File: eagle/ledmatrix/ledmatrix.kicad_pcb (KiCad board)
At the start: 2 copper layers, 100 x 160 mm, 65 parts, among them P1 CONN_01X05, P2 CONN_01X05, Q1 BSS138, Q10 BSS138, Q11 BSS138, Q12 BSS138, Q13 BSS138, Q14 BSS138, Q15 BSS138, Q16 BSS138, Q17 BSS138, Q18 BSS138, Q19 BSS138, Q2 BSS138, Q20 BSS138, Q3 BSS138, Q4 BSS138, Q5 BSS138, Q6 BSS138, Q7 BSS138, Q8 BSS138, Q9 BSS138, U1 74HC595, U2 74HC595, U3 74HC595

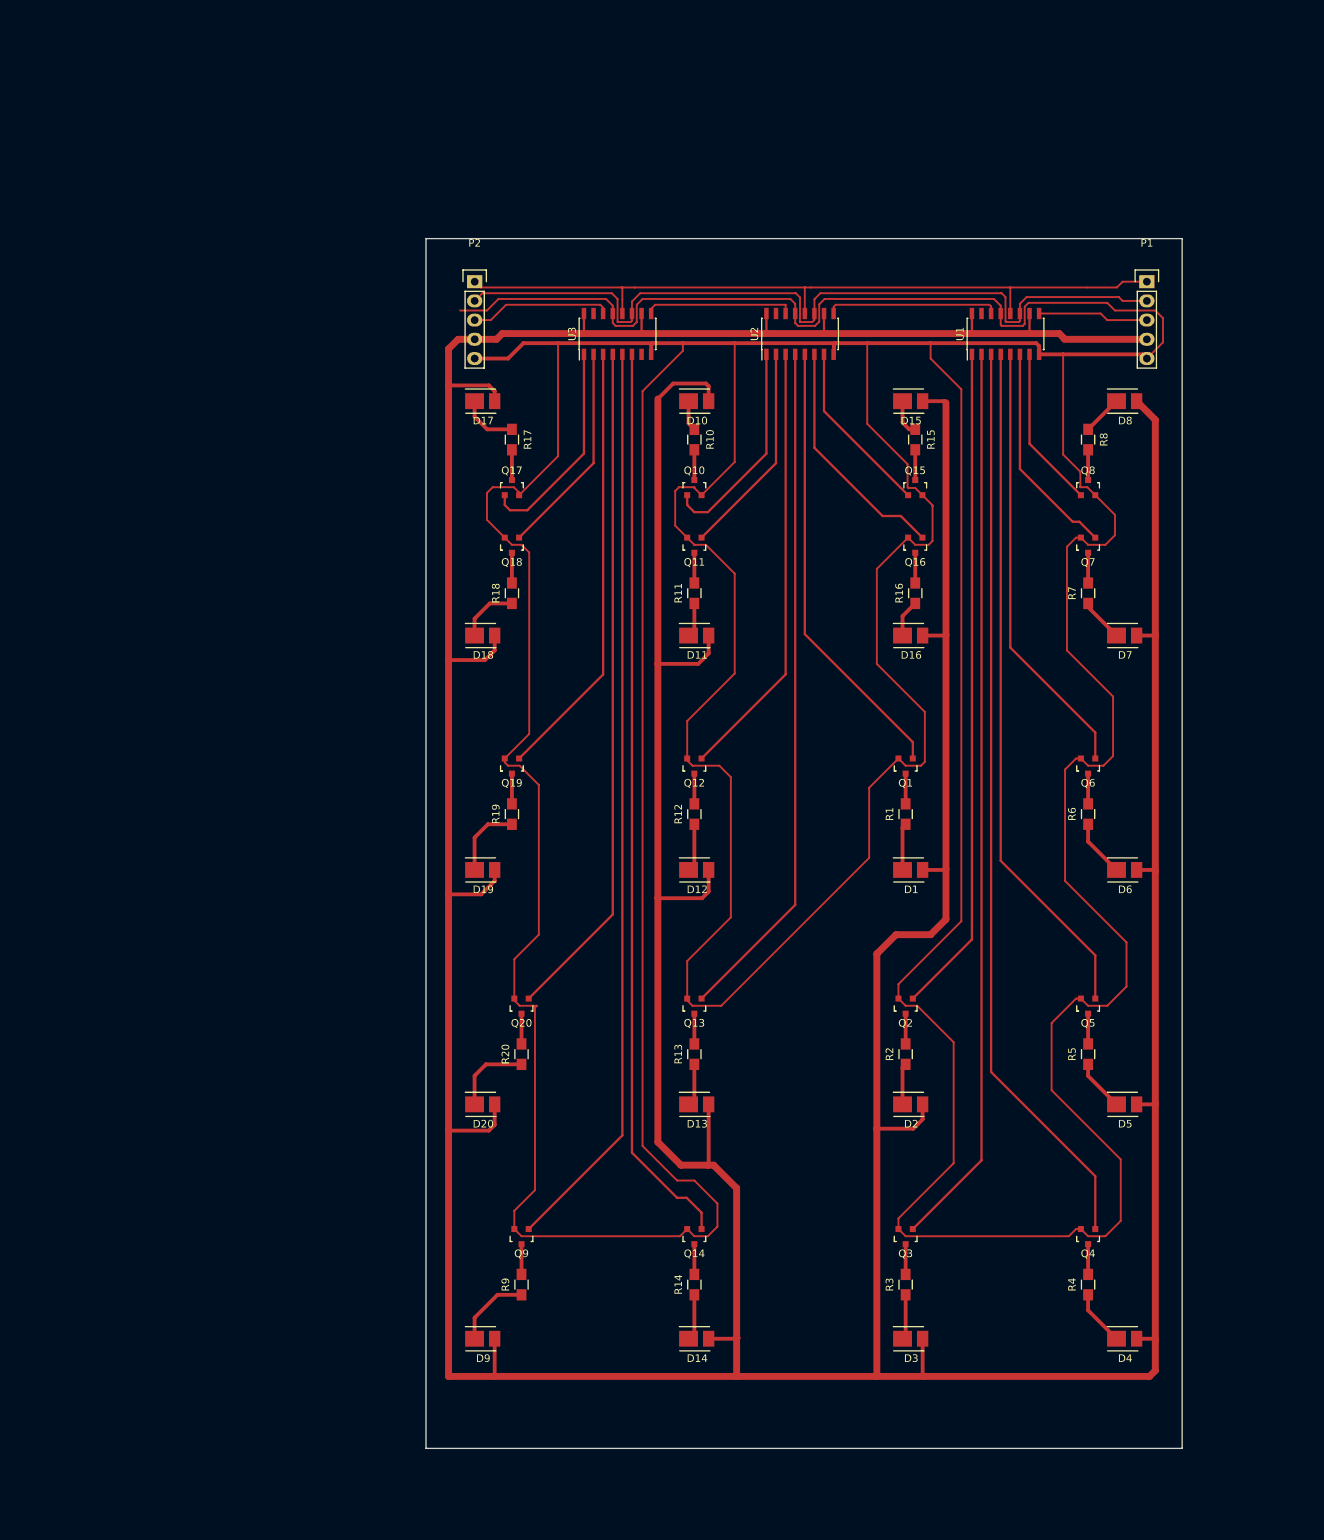
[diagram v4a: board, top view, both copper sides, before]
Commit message: adds ground fill.
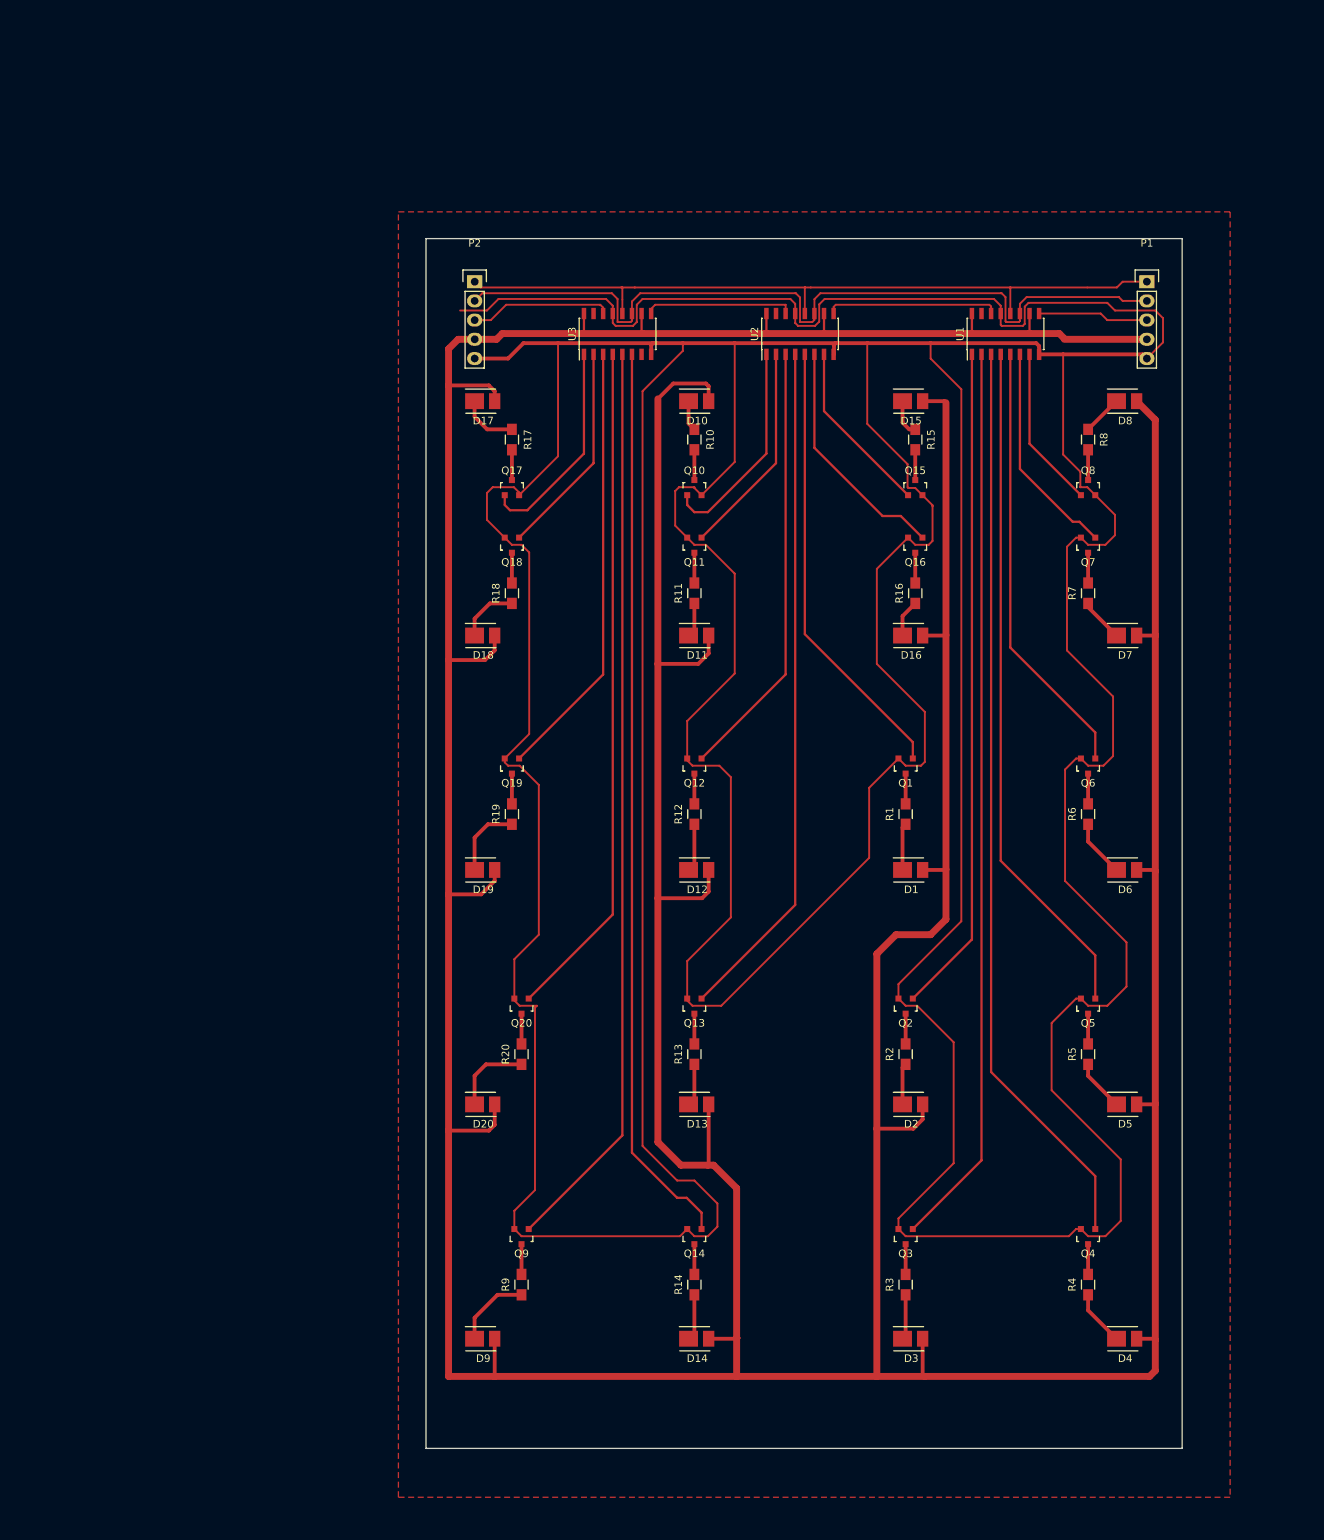
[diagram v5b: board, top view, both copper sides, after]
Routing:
- added copper zone on F.Cu, net GND
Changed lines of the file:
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@@
     (links 126)
     (no_connects 0)
-    (area 51.842599 23.343799 151.992601 183.493801)
+    (area 48.26502 19.8831 158.265021 189.883101)
     (thickness 1.6)
     (drawings 6)
@@
     (visible_elements FFFFFF7F)
     (pcbplotparams
-      (layerselection 0x00030_80000001)
+      (layerselection 0x02000_00000001)
       (usegerberextensions false)
       (excludeedgelayer true)
@@
       (padsonsilk false)
       (subtractmaskfromsilk false)
-      (outputformat 1)
+      (outputformat 4)
       (mirror false)
-      (drillshape 1)
+      (drillshape 0)
       (scaleselection 1)
       (outputdirectory ""))
@@
   (segment (start 143.21027 44.91865) (end 139.47902 48.6499) (width 0.508) (layer F.Cu) (net 8))
   (segment (start 118.90502 58.8391) (end 118.90502 58.68666) (width 0.254) (layer F.Cu) (net 9))
-  (segment (start 118.90502 58.68666) (end 117.56902 57.35066) (width 0.254) (layer F.Cu) (net 9) (status 800000))
-  (segment (start 117.56902 57.35066) (end 116.61902 56.40066) (width 0.254) (layer F.Cu) (net 9) (status 400000))
+  (segment (start 118.90502 58.68666) (end 117.56902 57.35066) (width 0.254) (layer F.Cu) (net 9))
+  (segment (start 117.56902 57.35066) (end 116.61902 56.40066) (width 0.254) (layer F.Cu) (net 9))
   (segment (start 110.26902 47.9171) (end 110.26902 37.2491) (width 0.254) (layer F.Cu) (net 9))
   (segment (start 115.60302 53.2511) (end 110.26902 47.9171) (width 0.254) (layer F.Cu) (net 9))
@@
   (segment (start 99.47402 32.1691) (end 99.47402 32.1691) (width 0.25) (layer F.Cu) (net 72))
   (segment (start 81.69402 32.7025) (end 81.69402 33.3299) (width 0.25) (layer F.Cu) (net 72))
+  (zone (net 9) (net_name GND) (layer F.Cu) (hatch edge 0.508)
+    (connect_pads (clearance 0.508))
+    (min_thickness 0.254)
+    (fill (arc_segments 16) (thermal_gap 0.508) (thermal_bridge_width 0.508))
+    (polygon
+      (pts
+        (xy 158.26502 189.8831) (xy 48.26502 189.8831) (xy 48.26502 19.8831) (xy 158.26502 19.8831)
+      )
+    )
+  )
 )

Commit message: regenrates fill. Adds rendered board.
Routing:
- net GND: track 1041.4 -> 1065.4 mm
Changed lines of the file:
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@@
     (thickness 1.6)
     (drawings 6)
-    (tracks 506)
+    (tracks 517)
     (zones 0)
     (modules 65)
@@
     (user_trace_width 0.9144)
     (trace_clearance 0.2)
-    (zone_clearance 0.508)
+    (zone_clearance 0.4064)
     (zone_45_only no)
     (trace_min 0.2)
@@
     (visible_elements FFFFFF7F)
     (pcbplotparams
-      (layerselection 0x02000_00000001)
+      (layerselection 0x00000_00000001)
       (usegerberextensions false)
       (excludeedgelayer true)
@@
       (padsonsilk false)
       (subtractmaskfromsilk false)
-      (outputformat 4)
+      (outputformat 2)
       (mirror false)
       (drillshape 0)
@@
   (segment (start 143.23732 44.91865) (end 143.21027 44.91865) (width 0.508) (layer F.Cu) (net 8))
   (segment (start 143.21027 44.91865) (end 139.47902 48.6499) (width 0.508) (layer F.Cu) (net 8))
+  (segment (start 149.38502 33.9471) (end 149.38502 30.8991) (width 0.254) (layer F.Cu) (net 9))
+  (segment (start 148.87702 30.3911) (end 144.81302 30.3911) (width 0.254) (layer F.Cu) (net 9))
+  (segment (start 149.38502 30.8991) (end 148.87702 30.3911) (width 0.254) (layer F.Cu) (net 9))
+  (segment (start 56.42102 32.9311) (end 56.42102 35.4711) (width 0.254) (layer F.Cu) (net 9))
+  (segment (start 76.61402 32.2961) (end 75.72502 31.4071) (width 0.254) (layer F.Cu) (net 9))
+  (segment (start 75.72502 31.4071) (end 61.50102 31.4071) (width 0.254) (layer F.Cu) (net 9))
+  (segment (start 61.50102 31.4071) (end 59.97702 32.9311) (width 0.254) (layer F.Cu) (net 9))
+  (segment (start 59.97702 32.9311) (end 56.42102 32.9311) (width 0.254) (layer F.Cu) (net 9))
+  (segment (start 76.61402 33.3299) (end 76.61402 32.2961) (width 0.254) (layer F.Cu) (net 9))
+  (segment (start 56.42102 35.4711) (end 59.97702 35.4711) (width 0.254) (layer F.Cu) (net 9))
+  (segment (start 81.05902 31.4071) (end 81.05902 34.9631) (width 0.254) (layer F.Cu) (net 9))
+  (segment (start 105.18902 31.4071) (end 105.18902 34.9631) (width 0.254) (layer F.Cu) (net 9))
+  (segment (start 132.36702 31.9151) (end 132.36702 34.9631) (width 0.254) (layer F.Cu) (net 9))
   (segment (start 118.90502 58.8391) (end 118.90502 58.68666) (width 0.254) (layer F.Cu) (net 9))
   (segment (start 118.90502 58.68666) (end 117.56902 57.35066) (width 0.254) (layer F.Cu) (net 9))
@@
   (segment (start 127.92202 32.2961) (end 127.92202 33.3299) (width 0.254) (layer F.Cu) (net 9))
   (segment (start 104.63022 31.4071) (end 103.91902 32.1183) (width 0.254) (layer F.Cu) (net 9))
-  (segment (start 127.03302 31.4071) (end 104.63022 31.4071) (width 0.254) (layer F.Cu) (net 9))
+  (segment (start 127.03302 31.4071) (end 105.18902 31.4071) (width 0.254) (layer F.Cu) (net 9))
+  (segment (start 105.18902 31.4071) (end 104.63022 31.4071) (width 0.254) (layer F.Cu) (net 9))
   (segment (start 127.92202 32.2961) (end 127.03302 31.4071) (width 0.254) (layer F.Cu) (net 9))
   (segment (start 103.91902 32.1183) (end 103.91902 34.4043) (width 0.254) (layer F.Cu) (net 9))
@@
   (segment (start 131.09702 34.7091) (end 131.09702 32.4231) (width 0.254) (layer F.Cu) (net 9))
   (segment (start 131.09702 32.4231) (end 131.60502 31.9151) (width 0.254) (layer F.Cu) (net 9))
-  (segment (start 131.60502 31.9151) (end 142.01902 31.9151) (width 0.254) (layer F.Cu) (net 9))
+  (segment (start 131.60502 31.9151) (end 132.36702 31.9151) (width 0.254) (layer F.Cu) (net 9))
+  (segment (start 132.36702 31.9151) (end 142.01902 31.9151) (width 0.254) (layer F.Cu) (net 9))
   (segment (start 142.01902 31.9151) (end 143.03502 32.9311) (width 0.254) (layer F.Cu) (net 9))
   (segment (start 143.03502 32.9311) (end 148.36902 32.9311) (width 0.254) (layer F.Cu) (net 9))
@@
   (segment (start 149.38502 33.9471) (end 149.38502 37.1475) (width 0.254) (layer F.Cu) (net 9))
   (segment (start 149.38502 37.1475) (end 147.25142 39.2811) (width 0.254) (layer F.Cu) (net 9))
-  (segment (start 76.61402 33.3299) (end 76.61402 32.2961) (width 0.254) (layer F.Cu) (net 9))
-  (segment (start 59.97702 32.9311) (end 56.42102 32.9311) (width 0.254) (layer F.Cu) (net 9))
-  (segment (start 61.50102 31.4071) (end 59.97702 32.9311) (width 0.254) (layer F.Cu) (net 9))
-  (segment (start 75.72502 31.4071) (end 61.50102 31.4071) (width 0.254) (layer F.Cu) (net 9))
-  (segment (start 76.61402 32.2961) (end 75.72502 31.4071) (width 0.254) (layer F.Cu) (net 9))
   (segment (start 100.74402 33.3299) (end 100.74402 32.0421) (width 0.254) (layer F.Cu) (net 9))
   (segment (start 76.61402 34.5821) (end 76.61402 33.3299) (width 0.254) (layer F.Cu) (net 9))
@@
   (segment (start 79.78902 32.1691) (end 79.78902 34.4551) (width 0.254) (layer F.Cu) (net 9))
   (segment (start 80.55102 31.4071) (end 79.78902 32.1691) (width 0.254) (layer F.Cu) (net 9))
-  (segment (start 100.10902 31.4071) (end 80.55102 31.4071) (width 0.254) (layer F.Cu) (net 9))
+  (segment (start 100.10902 31.4071) (end 81.05902 31.4071) (width 0.254) (layer F.Cu) (net 9))
+  (segment (start 81.05902 31.4071) (end 80.55102 31.4071) (width 0.254) (layer F.Cu) (net 9))
   (segment (start 100.74402 32.0421) (end 100.10902 31.4071) (width 0.254) (layer F.Cu) (net 9))
   (segment (start 100.87102 33.4569) (end 100.74402 33.3299) (width 0.254) (layer F.Cu) (net 9))
@@
   (segment (start 81.69402 32.7025) (end 81.69402 33.3299) (width 0.25) (layer F.Cu) (net 72))
   (zone (net 9) (net_name GND) (layer F.Cu) (hatch edge 0.508)
-    (connect_pads (clearance 0.508))
-    (min_thickness 0.254)
-    (fill (arc_segments 16) (thermal_gap 0.508) (thermal_bridge_width 0.508))
+    (connect_pads (clearance 0.4064))
+    (min_thickness 0.1524)
+    (fill yes (arc_segments 16) (thermal_gap 0.508) (thermal_bridge_width 0.508))
     (polygon
       (pts

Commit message: Adds copyright notice
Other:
- board size 100 x 160 mm -> 124.2 x 173.5 mm
- board text added: "(c) Balazs Racz 2017.01.09."
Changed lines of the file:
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@@
     (area 48.26502 19.8831 158.265021 189.883101)
     (thickness 1.6)
-    (drawings 6)
+    (drawings 21)
     (tracks 517)
     (zones 0)
@@
   )
   (setup
-    (last_trace_width 0.254)
+    (last_trace_width 0.25)
     (user_trace_width 0.254)
     (user_trace_width 0.3048)
@@
     (trace_clearance 0.2)
     (zone_clearance 0.4064)
-    (zone_45_only no)
+    (zone_45_only yes)
     (trace_min 0.2)
     (segment_width 0.2)
@@
     )
   )
+  (gr_text "(c) Balazs Racz\n2017.01.09." (at 101.88702 136.0551 90) (layer F.Cu)
+    (effects (font (size 1.5 1.5) (thickness 0.3)))
+  )
+  (gr_line (start 151.92502 179.2351) (end 151.92502 179.4891) (angle 90) (layer Edge.Cuts) (width 0.15))
+  (gr_line (start 51.84902 23.5331) (end 46.76902 23.5331) (angle 90) (layer Edge.Cuts) (width 0.15))
+  (gr_line (start 51.84902 19.9771) (end 51.84902 23.5331) (angle 90) (layer Edge.Cuts) (width 0.15))
+  (gr_line (start 51.84902 23.2791) (end 51.84902 19.9771) (angle 90) (layer Edge.Cuts) (width 0.15))
+  (gr_line (start 151.92502 23.5331) (end 151.92502 20.2311) (angle 90) (layer Edge.Cuts) (width 0.15))
+  (gr_line (start 157.25902 23.5331) (end 151.92502 23.5331) (angle 90) (layer Edge.Cuts) (width 0.15))
+  (gr_line (start 151.92502 23.5331) (end 157.25902 23.5331) (angle 90) (layer Edge.Cuts) (width 0.15))
+  (gr_line (start 151.92502 183.5531) (end 151.92502 192.1891) (angle 90) (layer Edge.Cuts) (width 0.15))
+  (gr_line (start 163.86302 183.5531) (end 151.92502 183.5531) (angle 90) (layer Edge.Cuts) (width 0.15))
+  (gr_line (start 151.92502 183.5531) (end 163.86302 183.5531) (angle 90) (layer Edge.Cuts) (width 0.15))
+  (gr_line (start 51.84902 183.5531) (end 51.84902 193.4591) (angle 90) (layer Edge.Cuts) (width 0.15))
+  (gr_line (start 51.59502 183.5531) (end 51.84902 183.5531) (angle 90) (layer Edge.Cuts) (width 0.15))
+  (gr_line (start 39.65702 183.5531) (end 51.59502 183.5531) (angle 90) (layer Edge.Cuts) (width 0.15))
+  (gr_line (start 47.02302 183.5531) (end 39.65702 183.5531) (angle 90) (layer Edge.Cuts) (width 0.15))
   (gr_line (start 51.9176 28.4188) (end 151.9176 28.4188) (angle 90) (layer Dwgs.User) (width 0.2))
   (gr_line (start 51.9176 178.4188) (end 151.9176 178.4188) (angle 90) (layer Dwgs.User) (width 0.2))
@@
       )
     )
+    (polygon
+      (pts        (xy 97.82302 125.3871) (xy 97.82302 146.7231) (xy 106.20502 146.7231) (xy 106.20502 125.3871)
+      )
+    )
